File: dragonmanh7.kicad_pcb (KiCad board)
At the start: 4 copper layers, 135.6 x 54.6 mm, 115 parts, among them J1 USB_B, J10 Conn_02x12_Odd_Even, J11 Conn_02x03_Odd_Even, J12 VBAT+, J13 Conn_02x05_Odd_Even, J14 VBATG, J15 Conn_02x02_Odd_Even, J18 Conn_02x05_Odd_Even, J2 73725-0110BLF, J3 RJ45_Amphenol_RJMG1BD3B8K1ANR, J4 Micro_SD_Card, J5 Screw_Terminal_01x06, J6 Conn_02x12_Odd_Even, J7 USB_B, J8 Screw_Terminal_01x02, J9 Conn_02x12_Odd_Even, SW1 RESET, SW2 PC13, U1 STM32H743VITx, U10 USBLC6-2SC6, U11 SN6505, U12 TCAN332, U13 ISL83483, U14 MIC2005A, U2 KSZ8081RNA, U3 ISO1050DUB, U4 ISO3082DW, U5 S25FL127SABMFI101, U6 AP63203, U7 USBLC6-2SC6, U8 STM32F042F6Px, U9 USBLC6-2SC6, Y1 8MHz, Y2 32.768KHz, Y3 25MHz

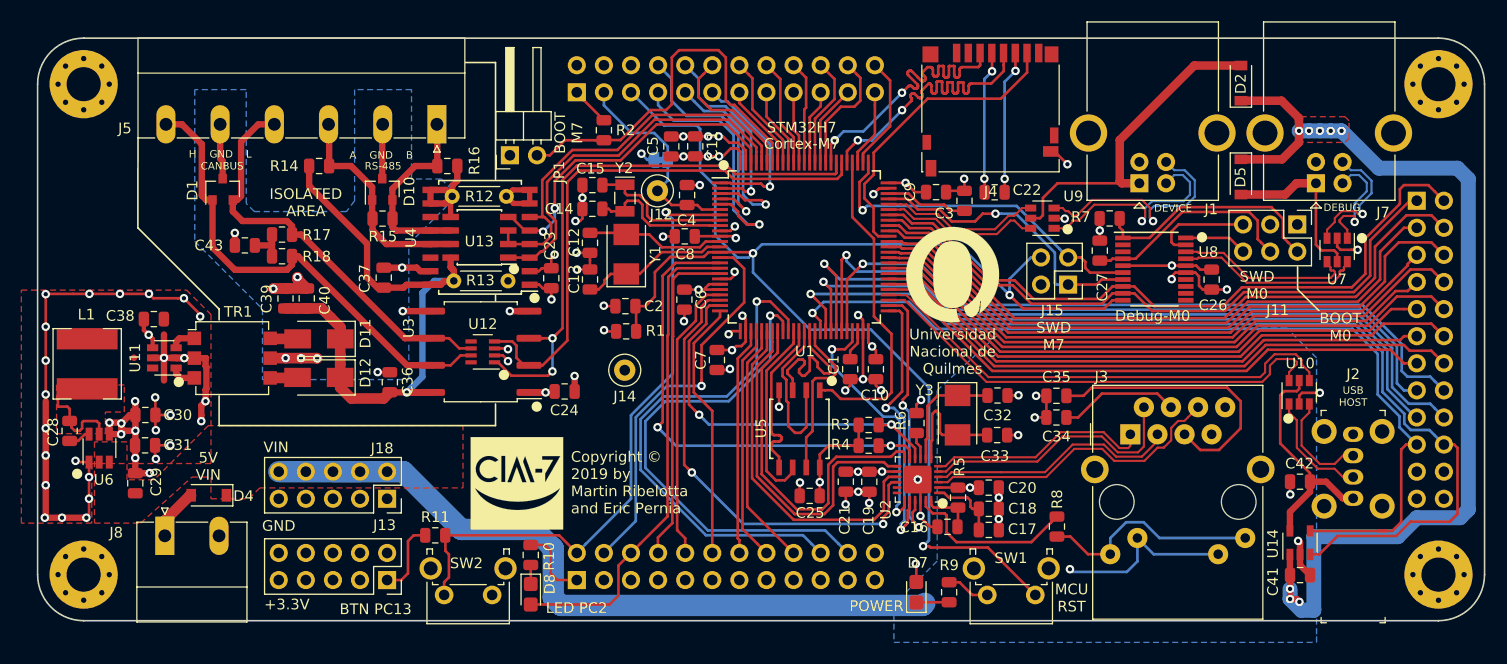
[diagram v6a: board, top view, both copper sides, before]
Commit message: Minor changes in some traces
Signed-off-by: Martin Ribelotta <martinribelotta@gmail.com>
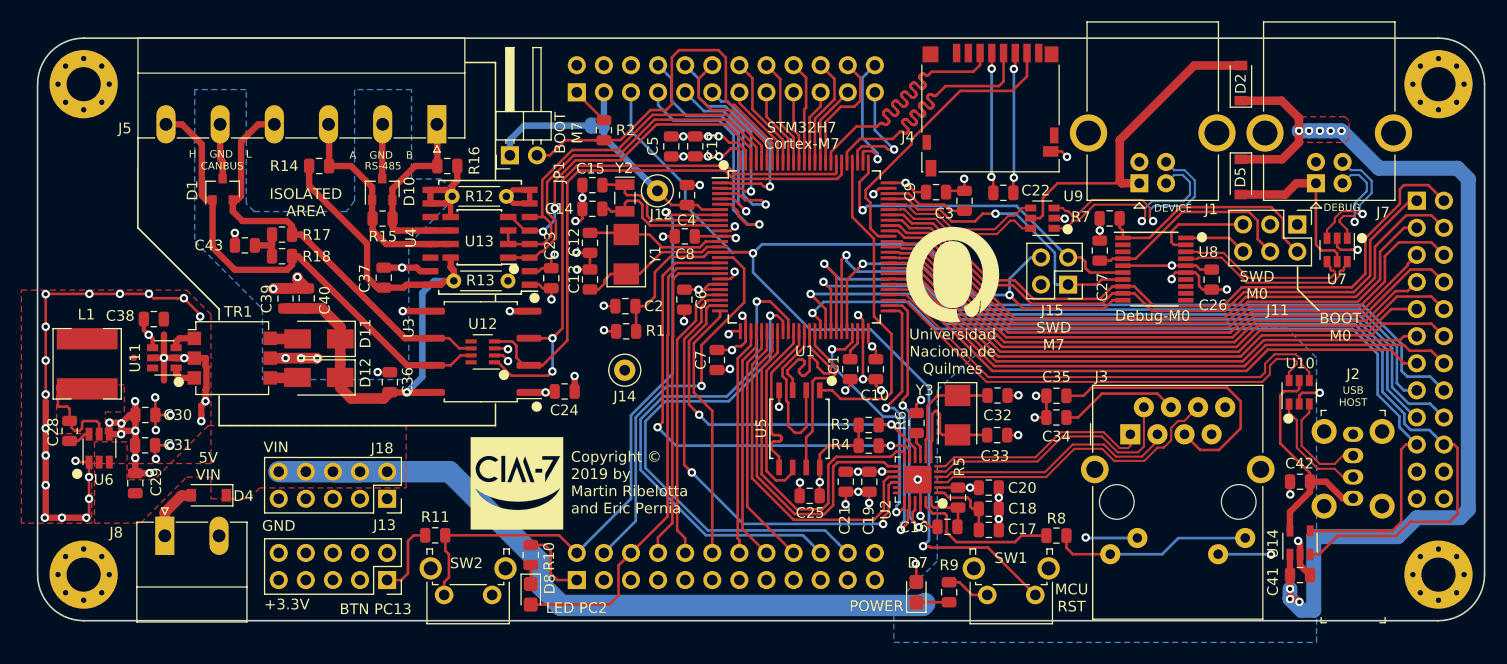
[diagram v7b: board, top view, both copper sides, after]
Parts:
- moved JP5 6.78 mm to (111.1, 36.1)
- moved R8 0.85 mm to (154.2, 74.6), turned to 180 degrees
- moved C22 0.81 mm to (149.2, 42.4)
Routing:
- net GND: track 168.4 -> 160.4 mm, vias 59 -> 60
- net +3V3: track 160.8 -> 168.7 mm, vias 49 -> 48
- net /PC10: track 7.26 -> 10.9 mm, vias 0 -> 1
- net Net-(J3-PadL1): track 21.1 -> 18.8 mm
- net /~RESET: track 133.3 -> 131.2 mm
- net +BATT: track 20.0 -> 17.9 mm
- net /PA15: track 10.8 -> 12.8 mm, vias 0 -> 1
- net /ETH_LED: track 16.2 -> 14.5 mm
- net VDC: track 165.6 -> 164.1 mm
- net /SDMMC_D0: track 29.0 -> 27.8 mm
- net /SDMMC_CMD: track 29.0 -> 27.8 mm, vias 2 -> 0
- net /SDMMC_CLK: track 28.9 -> 27.7 mm, vias 2 -> 0

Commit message: Remove non-isolated version of board
Signed-off-by: Martin Ribelotta <martinribelotta@gmail.com>
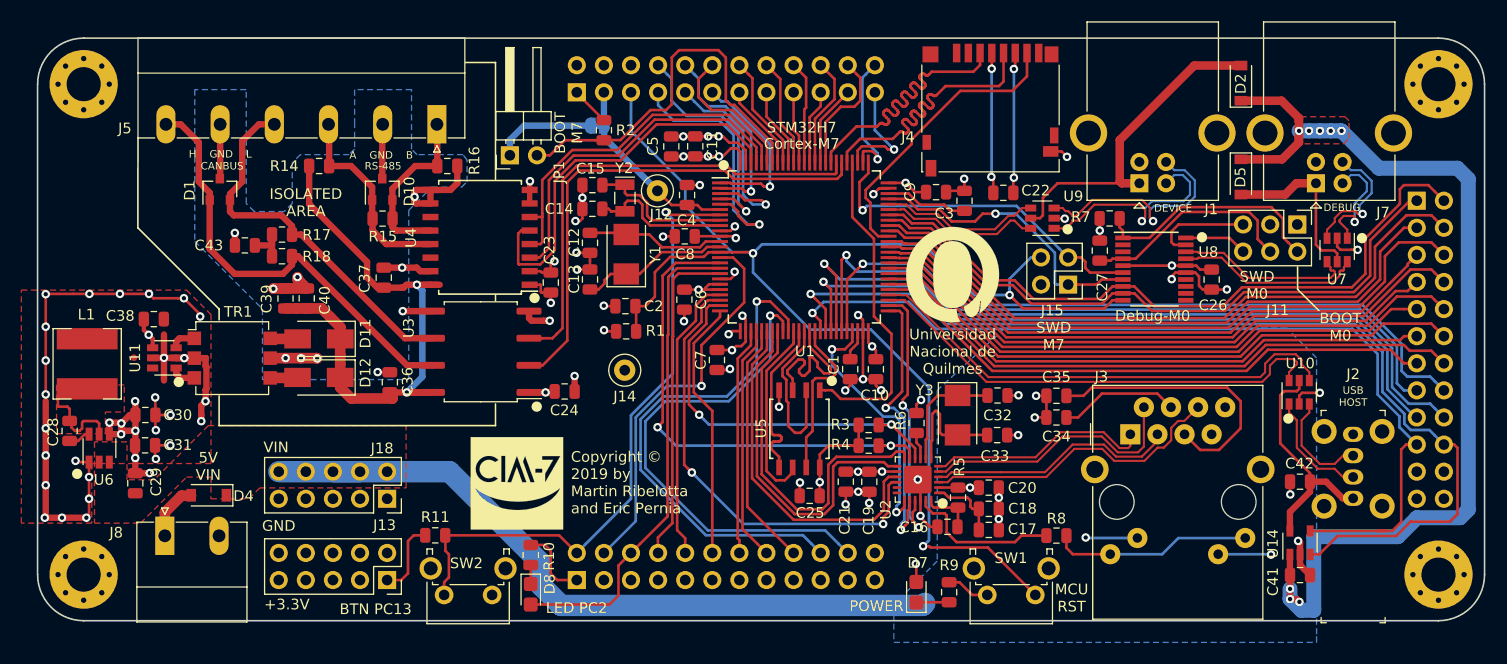
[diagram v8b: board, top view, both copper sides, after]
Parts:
- removed R12, R13: 0R, Resistor_THT:R_Axial_DIN0204_L3.6mm_D1.6mm_P5.08mm_Horizontal
- removed U12: TCAN332, Package_TO_SOT_SMD:SOT-23-8
- removed U13: ISL83483, Package_SO:SOIC-8_3.9x4.9mm_P1.27mm
- moved C23 0.41 mm to (106.8, 50.9)
- moved D1 0.26 mm to (75.8, 42.1)
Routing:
- net /CAN_TX: track 54.2 -> 45.0 mm, vias 2 -> 0
- net +5P: track 61.3 -> 54.9 mm, vias 1 -> 2
- net /RS485_TX: track 31.9 -> 37.3 mm, vias 2 -> 0
- net GND: track 160.4 -> 155.4 mm
- net /CAN_RX: track 52.0 -> 47.2 mm
- net /RS485_DE: track 38.4 -> 34.2 mm
- net /CAN_L: track 39.0 -> 35.1 mm
- net /CAN_H: track 45.3 -> 41.4 mm
- net /RS485_RX: track 35.4 -> 32.9 mm
- net /RS485_B: track 20.7 -> 18.9 mm
- net /RS485_A: track 18.2 -> 16.3 mm
- net GNDPWR: track 39.8 -> 38.6 mm, vias 9 -> 10
- net +3V3: track 168.7 -> 167.8 mm, vias 48 -> 47
